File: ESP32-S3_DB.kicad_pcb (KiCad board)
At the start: 4 copper layers, 123.5 x 56.5 mm, 157 parts, among them CN1 JST_Battery, J1 TYPE-C-31-M12_13, J10 U2RS485_TX, J11 CAN_TX, J12 CAN_RX, J14 Conn_01x06, J15 Conn_01x10, J16 Conn_01x08, J17 U2RS485_RX, J18 U2RS485_DE_~{RE}, J19 U2RS485_TX, J2 A - B, J20 U2RS485_RX, J21 U2U, J22 PROG_Default, J3 H - L, J4 TYPE-C-31-M12_13, J5 EXT_LOAD, J6 R4_TX, J7 R4_RX, J8 Micro_SD_Card_Det1, J9 Conn_01x06, SW1 RESET, SW2 BOOT, SW3 ON/OFF, U1 ESP32-S3FH4R2, U2 UMH3N, U3 IP5306, U4 CH340X, U5 LD1117DT33CTR, U6 SP3071EEN-L/TR, U7 ATA6561-GAQW-N, X1 32.768KHz, Y1 40MHz

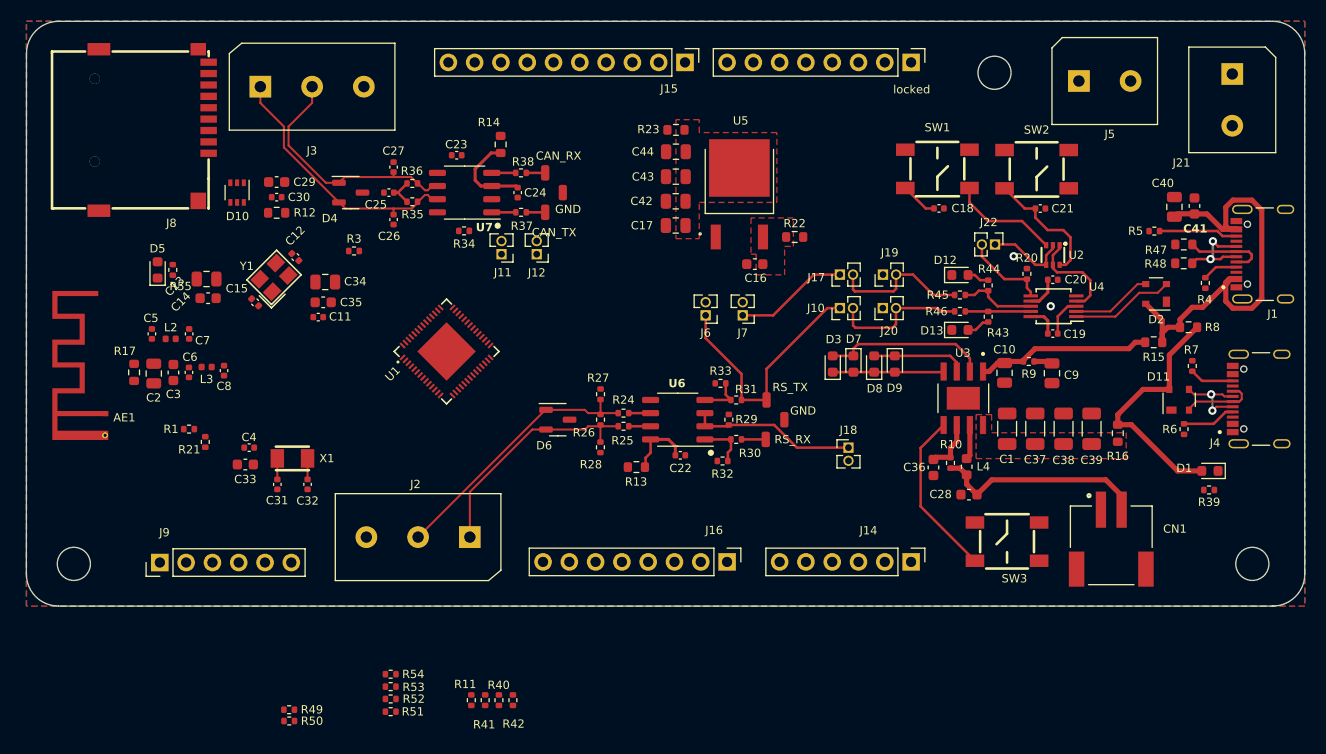
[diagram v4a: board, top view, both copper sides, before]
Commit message: Completed routing for all GPIO pins
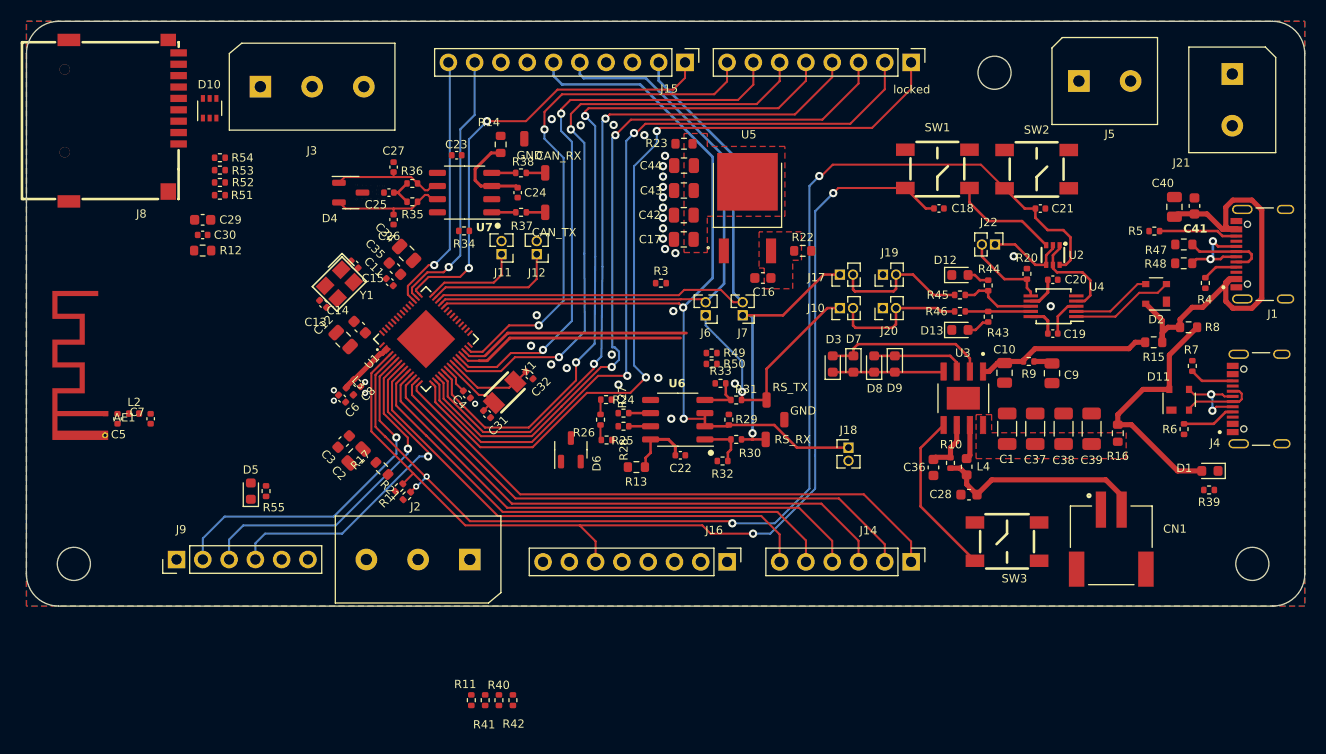
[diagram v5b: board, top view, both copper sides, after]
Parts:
- removed C33: 1uF, ESP32-S3_Dev_Board:C_0603_1608Metric
- moved R50 53.4 mm to (158.7, 119.1)
- moved R49 53.4 mm to (158.7, 118.0)
- moved R52 52.6 mm to (111.2, 101.6)
- moved R53 52.6 mm to (111.2, 100.4)
- moved R54 52.6 mm to (111.2, 99.2)
- moved R51 52.6 mm to (111.2, 102.8)
- moved R3 29.8 mm to (153.8, 111.3)
- moved R17 25.7 mm to (126.8, 129.2), turned to 135 degrees
- moved C32 23.9 mm to (141.1, 120.2), turned to -45 degrees
- moved D5 23.2 mm to (114.2, 131.4)
- moved R55 23.2 mm to (115.7, 131.4)
- moved C4 21.6 mm to (135.1, 122.0), turned to -45 degrees
- moved X1 21.5 mm to (138.7, 121.8), turned to 45 degrees
- moved C31 21.4 mm to (137.0, 124.0), turned to -45 degrees
- moved C2 21.1 mm to (124.3, 128.0), turned to -135 degrees
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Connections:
- J10 pad 2: /U2U_RXD -> /U2U_TXD
- J14 pad 1: /GPIO11 -> /GPIO9
- J14 pad 2: /GPIO10 -> /GPIO8
- J14 pad 3: /GPIO9 -> /GPIO7
- J14 pad 4: /GPIO8 -> /GPIO6
- J14 pad 5: /GPIO7 -> /GPIO5
- J14 pad 6: /GPIO6 -> /GPIO4
- J15 pad 1: /GPIO9 -> /GPIO38
- J15 pad 10: /GPIO39 -> /GPIO40
- J15 pad 2: /EXTERNAL CONNECTORS/GPIO14 -> /RS485_RX/GPIO34
- J15 pad 5: /EXTERNAL CONNECTORS/GPIO17 -> /RS485_TX/GPIO33
- J15 pad 6: /GPIO18 -> /RS485_~{RE}_DE/GPIO35
- J15 pad 9: /GPIO38 -> /GPIO39
- J17 pad 2: /U2U_TXD -> /U2U_RXD
- J6 pad 2: /RS-485_RX/GPIO46 -> /RS485_TX/GPIO33
- J7 pad 2: /RS-485_TX/GPIO45 -> /RS485_RX/GPIO34
- J9 pad 5: /GPIO4 -> unconnected-(J9-Pin_5-Pad5)
- J9 pad 6: /GPIO5 -> unconnected-(J9-Pin_6-Pad6)
- R51 pad 1: /~{MCU_SL_CS} -> /MCU_SL_CLK
- R51 pad 2: unconnected-(R51-Pad2) -> Net-(U1-MTDI)
- R52 pad 1: /MCU_SL_MISO -> /MCU_SL_MOSI
- R52 pad 2: unconnected-(R52-Pad2) -> Net-(U1-MTMS)
- R53 pad 1: /MCU_SL_CLK -> /MCU_SL_MISO
- R53 pad 2: unconnected-(R53-Pad2) -> Net-(U1-GPIO45)
- R54 pad 1: /MCU_SL_MOSI -> /~{MCU_SL_CS}
- R54 pad 2: unconnected-(R54-Pad2) -> Net-(U1-GPIO46)
- U1 pad 19: /ESP32-S3/GPIO 14 -> /GPIO14
- U1 pad 23: /ESP32-S3/GPIO 17 -> /GPIO17
- U1 pad 27: /ESP32-S3/GPIO 21 -> /GPIO21
- U1 pad 38: /ESP32-S3/RS-485_TX/GPIO33 -> /RS485_~{RE}_DE/GPIO35
- U1 pad 39: /ESP32-S3/RS-485_RX/GPIO34 -> /RS485_TX/GPIO33
- U1 pad 40: /CAN_RXD/GPIO35 -> /RS485_RX/GPIO34
- U1 pad 41: /RS485_~{RE}_DE/GPIO35 -> /CAN_RXD/GPIO35
- U1 pad 47: /GPIO41 -> Net-(U1-MTDI)
- U1 pad 48: unconnected-(U1-MTMS-Pad48) -> Net-(U1-MTMS)
- U1 pad 51: unconnected-(U1-GPIO45-Pad51) -> Net-(U1-GPIO45)
- U1 pad 52: unconnected-(U1-GPIO46-Pad52) -> Net-(U1-GPIO46)
- locked pad 1: /GPIO21 -> /GPIO10
- locked pad 2: /GPIO33 -> /GPIO11
- locked pad 3: /GPIO34 -> /GPIO12
- locked pad 4: /GPIO35 -> /GPIO13
- locked pad 5: /GPIO36 -> /GPIO14
- locked pad 6: /GPIO37 -> /GPIO17
- locked pad 7: /EXTERNAL CONNECTORS/CAN_RX/GPIO8 -> /GPIO18
- locked pad 8: /EXTERNAL CONNECTORS/CAN_TX/GPIO7 -> /GPIO21
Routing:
- net /BOOT: track 12.3 -> 119.1 mm, vias 0 -> 4
- net /RESET: track 14.1 -> 113.2 mm, vias 0 -> 2
- net /GPIO10: track 0.00 -> 80.9 mm, vias 0 -> 2
- net /GPIO11: track 0.00 -> 77.0 mm, vias 0 -> 2
- net /GPIO12: track 0.00 -> 73.7 mm, vias 0 -> 2
- net /RS485_~{RE}_DE/GPIO35: track 16.1 -> 88.0 mm, vias 0 -> 2
- net /GPIO13: track 0.00 -> 70.1 mm, vias 0 -> 2
- net /GPIO14: track 0.00 -> 69.2 mm, vias 0 -> 2
- net /GPIO17: track 0.00 -> 59.4 mm, vias 0 -> 2
- net /RS485_TX/GPIO33: track 0.00 -> 59.1 mm
- net /RS485_RX/GPIO34: track 0.00 -> 56.9 mm
- net /GPIO9: track 0.00 -> 56.7 mm
- net /GPIO18: track 0.00 -> 55.8 mm, vias 0 -> 2
- net /GPIO8: track 0.00 -> 55.0 mm
- net /GPIO7: track 0.00 -> 53.8 mm
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
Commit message: Completed RS485 and CAN routing
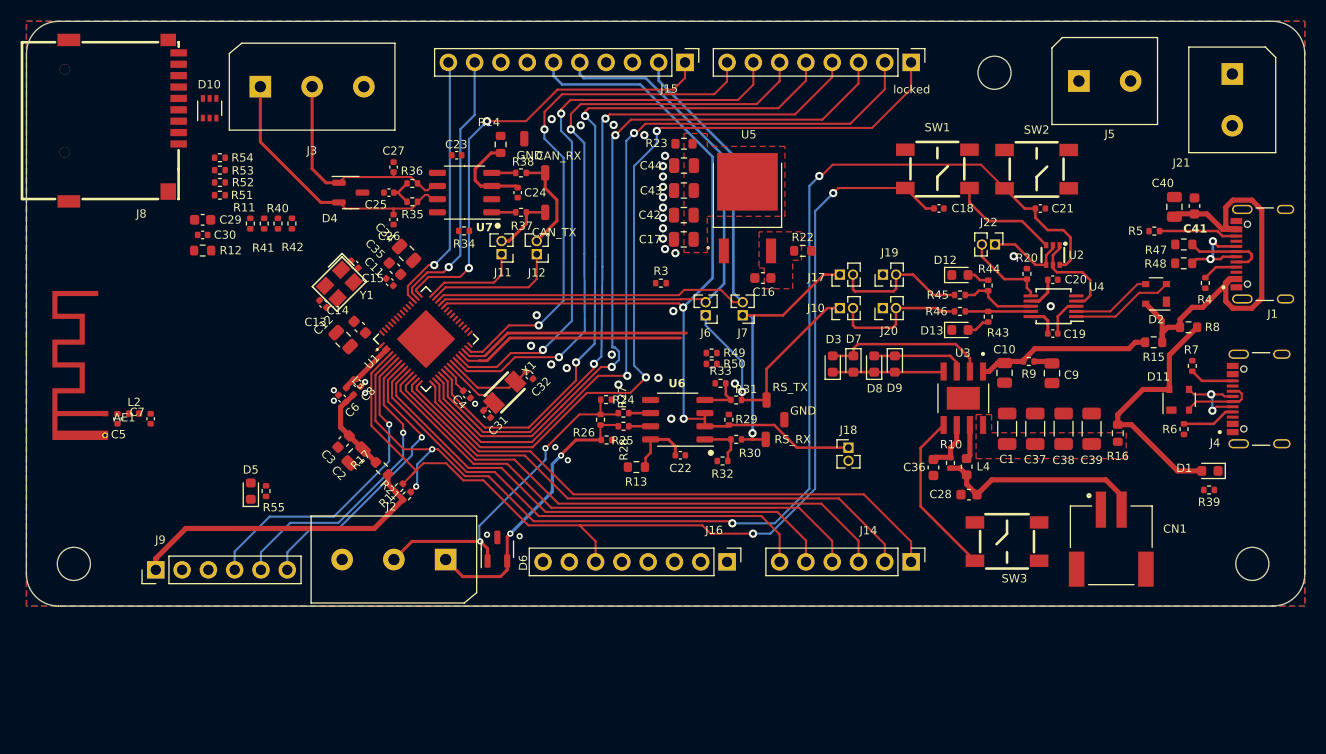
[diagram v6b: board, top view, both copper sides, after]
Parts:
- moved R40 50.8 mm to (116.8, 105.5)
- moved R11 50.8 mm to (114.1, 105.5)
- moved R41 50.8 mm to (115.5, 105.5)
- moved R42 50.8 mm to (118.2, 105.5)
- moved D6 11.9 mm to (138.0, 137.0)
- moved J2 2.34 mm to (128.0, 138.0)
- moved J9 2.24 mm to (105.0, 139.0)
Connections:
- D6 pad 2: /RS_485/COMM_RS485_B -> /CONN_RS485_B
- J9 pad 2: /GPIO1 -> GND
- J9 pad 3: /GPIO2 -> unconnected-(J9-Pin_3-Pad3)
- J9 pad 4: /GPIO3 -> /GPIO1
- J9 pad 5: unconnected-(J9-Pin_5-Pad5) -> /GPIO2
- J9 pad 6: unconnected-(J9-Pin_6-Pad6) -> /GPIO3
- R25 pad 2: /RS_485/COMM_RS485_B -> /CONN_RS485_B
- R26 pad 1: /RS_485/COMM_RS485_B -> /CONN_RS485_B
- R28 pad 2: /RS_485/COMM_RS485_B -> /CONN_RS485_B
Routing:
- net /CONN_RS485_A: track 1.44 -> 32.8 mm, vias 0 -> 2
- net /3V3: track 2.85 -> 33.2 mm
- net /CONN_RS485_B: track 0.00 -> 28.1 mm, vias 0 -> 2
- net /CONN_CANH: track 11.0 -> 26.4 mm
- net /CONN_CANL: track 10.9 -> 22.0 mm
- net Net-(C2-Pad1): track 0.00 -> 8.49 mm
- net /CAN_TRANS_RXD: track 1.83 -> 9.69 mm
- net /CAN_TRANS_TXD: track 1.82 -> 6.01 mm
- net /GPIO3: track 32.7 -> 28.6 mm
- net /GPIO1: track 34.6 -> 31.2 mm
- net /GPIO2: track 33.0 -> 29.9 mm
- net /BOOT: track 119.1 -> 121.5 mm
- net /RS_485/COMM_RS485_B: track 1.65 -> 0.00 mm
- net /RESET: track 113.2 -> 114.2 mm
- net Net-(U1-LNA_IN): track 0.03 -> 0.87 mm
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
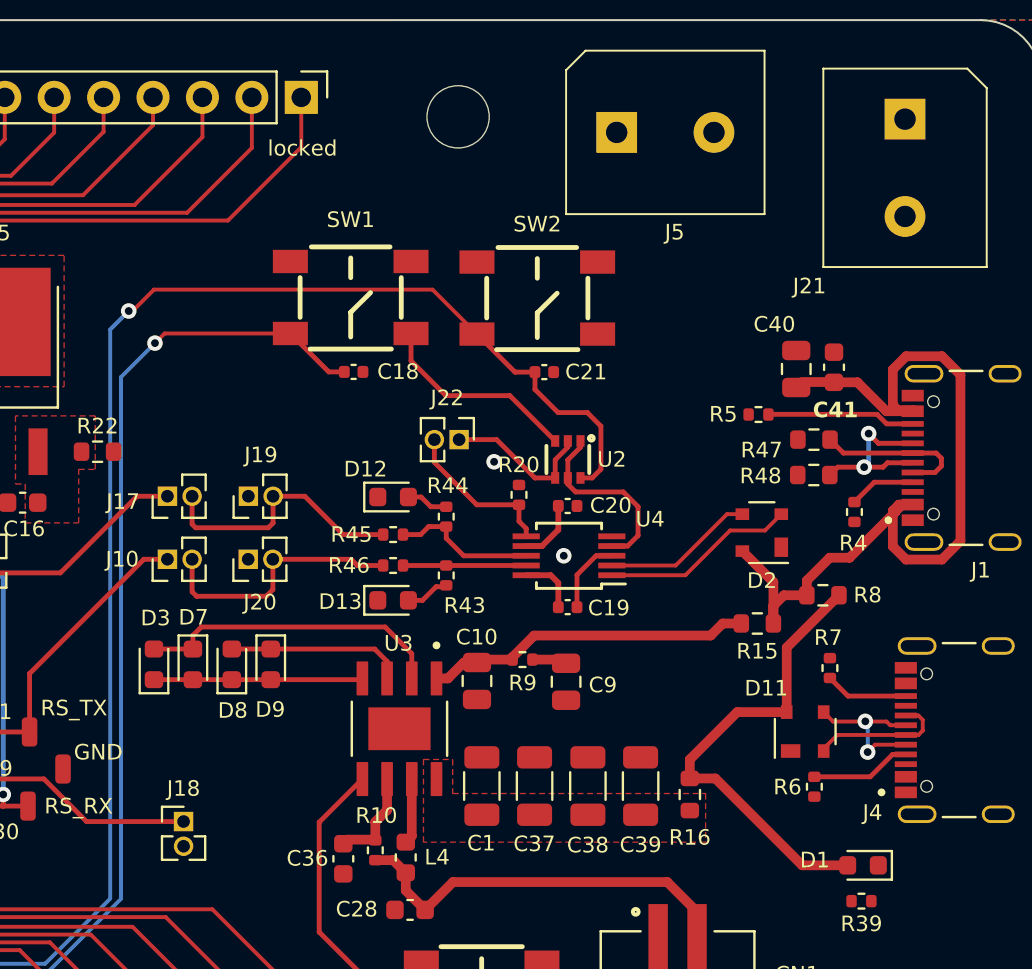
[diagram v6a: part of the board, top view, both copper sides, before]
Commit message: Completed routing for USB peripheral for CH340
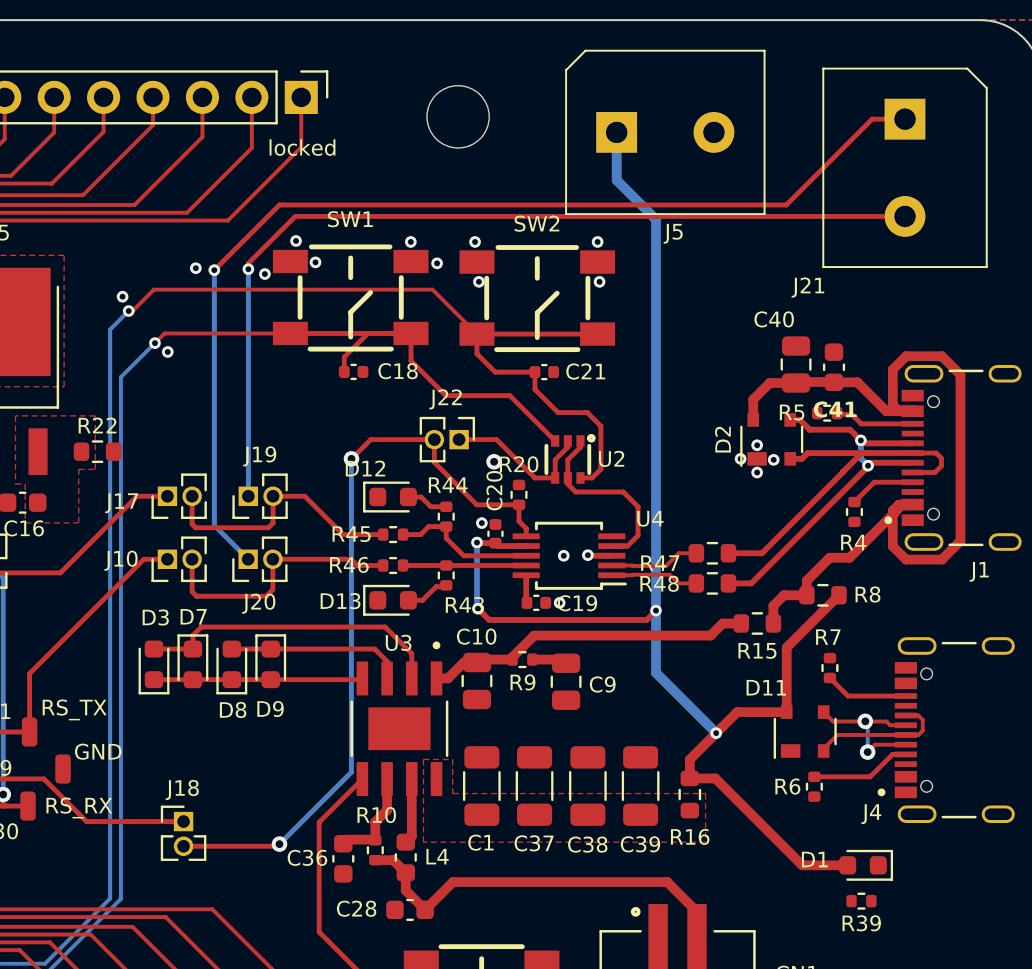
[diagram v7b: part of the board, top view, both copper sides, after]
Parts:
- moved R47 7.83 mm to (199.1, 113.4)
- moved R48 7.63 mm to (199.1, 115.0)
- moved D2 4.82 mm to (202.2, 107.5), turned to 90 degrees
- moved C20 3.98 mm to (187.9, 112.4), turned to -90 degrees
- moved R5 3.53 mm to (205.0, 106.2)
- moved C19 1.62 mm to (190.1, 116.0)
- moved C40 0.23 mm to (203.4, 103.7)
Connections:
- D2 pad 2: /D+ -> /INPUT POWER/DN
- D2 pad 3: /D- -> /INPUT POWER/DP
- J1 pad A6: Net-(J1-D+-PadA6) -> /INPUT POWER/DP
- J1 pad A7: Net-(J1-D--PadA7) -> /INPUT POWER/DN
- J1 pad B6: Net-(J1-D+-PadA6) -> /INPUT POWER/DP
- J1 pad B7: Net-(J1-D--PadA7) -> /INPUT POWER/DN
- J21 pad 1: /U2U_CONN_TX -> /U2U_CONN_RX
- J21 pad 2: /U2U_CONN_RX -> /U2U_CONN_TX
- R47 pad 1: Net-(J1-D--PadA7) -> /INPUT POWER/DN
- R48 pad 1: Net-(J1-D+-PadA6) -> /INPUT POWER/DP
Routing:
- net /U2U_CONN_RX: track 0.00 -> 54.3 mm, vias 0 -> 1
- net /U2U_CONN_TX: track 0.00 -> 46.7 mm, vias 0 -> 1
- net /5V: track 27.3 -> 72.7 mm, vias 0 -> 4
- net /TNOW: track 8.20 -> 39.2 mm, vias 0 -> 2
- net /INPUT POWER/DP: track 0.00 -> 20.3 mm, vias 0 -> 2
- net /INPUT POWER/DN: track 0.00 -> 19.3 mm
- net Net-(J1-D+-PadA6): track 8.81 -> 0.00 mm, vias 2 -> 0
- net Net-(J1-D--PadA7): track 8.13 -> 0.00 mm
- net /RESET: track 114.2 -> 121.6 mm
- net /BOOT: track 121.5 -> 128.3 mm
- net /D+: track 10.0 -> 4.54 mm
- net /INPUT POWER/CC2: track 7.62 -> 4.11 mm
- net /D-: track 7.80 -> 4.63 mm
- net GND: track 3.86 -> 1.41 mm, vias 51 -> 70
- net /USB-TO-UART/V3: track 3.06 -> 1.44 mm
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
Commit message: Merge changes upstream
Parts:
- removed C34: 10uF, ESP32-S3_Dev_Board:C_0805_2012Metric
- removed C35: 1uF, ESP32-S3_Dev_Board:C_0603_1608Metric
- removed R3: 500, ESP32-S3_Dev_Board:R_0402_1005Metric
- added R2: 270, ESP32-S3_Dev_Board:R_0402_1005Metric, F.Cu at (137.7, 113.8)
- moved J9 63.1 mm to (162.9, 113.9), turned to 0 degrees
- moved R52 47.6 mm to (151.3, 127.1), turned to 135 degrees
- moved R51 46.1 mm to (150.1, 127.6), turned to 135 degrees
- moved R54 44.7 mm to (148.3, 124.1), turned to 135 degrees
- moved R53 43.9 mm to (147.5, 125.0), turned to 135 degrees
- moved R28 40.8 mm to (107.7, 126.9), turned to 90 degrees
- moved R27 40.8 mm to (107.7, 121.8), turned to 90 degrees
- moved R50 40.3 mm to (199.0, 119.5), turned to 90 degrees
- moved C22 40.2 mm to (115.5, 127.7)
- moved R13 40.2 mm to (111.2, 128.9)
- moved R24 40.2 mm to (110.0, 123.6)
- moved R25 40.2 mm to (110.0, 124.9)
- moved R26 40.2 mm to (107.7, 124.3)
- moved R29 40.2 mm to (120.1, 124.3)
- moved R33 40.2 mm to (119.3, 120.8)
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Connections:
- net /CONN_CANH renamed /CAN_P
- net /CONN_CANL renamed /CAN_N
- net /CONN_RS485_A renamed /RS485_P
- net /CONN_RS485_B renamed /RS485_N
- net /RS_485/RS485_A renamed /RS_485/RS_485_P
- net /RS_485/RS485_B renamed /RS_485/RS_485_N
- net Net-(U1-XTAL_32K_N) renamed /ESP32-S3/XTALN
- net Net-(U1-XTAL_32K_P) renamed /ESP32-S3/XTALP
- D2 pad 2: /INPUT POWER/DN -> /D+
- D2 pad 3: /INPUT POWER/DP -> /D-
- J1 pad A6: /INPUT POWER/DP -> Net-(J1-D+-PadA6)
- J1 pad A7: /INPUT POWER/DN -> Net-(J1-D--PadA7)
- J1 pad B6: /INPUT POWER/DP -> Net-(J1-D+-PadA6)
- J1 pad B7: /INPUT POWER/DN -> Net-(J1-D--PadA7)
- J10 pad 2: /U2U_TXD -> /U2U_RXD
- J11 pad 1: /CAN_TXD/GPIO36 -> /CAN_TXD/GPIO7
- J12 pad 1: /CAN_RXD/GPIO35 -> /CAN_RXD/GPIO8
- J14 pad 1: /GPIO9 -> /GPIO6
- J14 pad 2: /GPIO8 -> /GPIO5
- J14 pad 3: /GPIO7 -> /GPIO4
- J14 pad 4: /GPIO6 -> /GPIO3
- J14 pad 5: /GPIO5 -> /GPIO2
- J14 pad 6: /GPIO4 -> /GPIO1
- J15 pad 1: /GPIO38 -> /GPIO9
- J15 pad 10: /GPIO40 -> /GPIO39
- J15 pad 2: /RS485_RX/GPIO34 -> /GPIO14
- J15 pad 4: unconnected-(J15-Pin_4-Pad4) -> /GPIO41
- J15 pad 5: /RS485_TX/GPIO33 -> /GPIO17
- J15 pad 6: /RS485_~{RE}_DE/GPIO35 -> /GPIO18
- J15 pad 8: unconnected-(J15-Pin_8-Pad8) -> /GPIO40
- J15 pad 9: /GPIO39 -> /GPIO38
- J16 pad 8: unconnected-(J16-Pin_8-Pad8) -> /R4_~{RE}_DE
- J17 pad 2: /U2U_RXD -> /U2U_TXD
- J18 pad 1: /RS485_~{RE}_DE/GPIO35 -> /R4_~{RE}_DE
- J21 pad 1: /U2U_CONN_RX -> /U2U_CONN_TX
- J21 pad 2: /U2U_CONN_TX -> /U2U_CONN_RX
- J6 pad 2: /RS485_TX/GPIO33 -> /RS-485_RX/GPIO46
- J7 pad 2: /RS485_RX/GPIO34 -> /RS-485_TX/GPIO45
- J9 pad 1: /3V3 -> /RS-485_TX/GPIO45
- J9 pad 2: GND -> /RS-485_RX/GPIO46
- J9 pad 4: /GPIO1 -> /3V3
- J9 pad 5: /GPIO2 -> unconnected-(J9-Pin_5-Pad5)
- J9 pad 6: /GPIO3 -> unconnected-(J9-Pin_6-Pad6)
- R29 pad 2: /RS485_~{RE}_DE/GPIO35 -> /R4_~{RE}_DE
- R47 pad 1: /INPUT POWER/DN -> Net-(J1-D--PadA7)
- R48 pad 1: /INPUT POWER/DP -> Net-(J1-D+-PadA6)
- R51 pad 1: /MCU_SL_CLK -> /~{MCU_SL_CS}
- R51 pad 2: Net-(U1-MTDI) -> Net-(U1-GPIO10)
- R52 pad 1: /MCU_SL_MOSI -> /MCU_SL_MISO
- R52 pad 2: Net-(U1-MTMS) -> Net-(U1-GPIO11)
- R53 pad 1: /MCU_SL_MISO -> /MCU_SL_CLK
- R53 pad 2: Net-(U1-GPIO45) -> Net-(U1-GPIO12)
- R54 pad 1: /~{MCU_SL_CS} -> /MCU_SL_MOSI
- R54 pad 2: Net-(U1-GPIO46) -> Net-(U1-GPIO13)
- U1 pad 12: /GPIO7 -> /U2U_RXD
- U1 pad 13: /GPIO8 -> /U2U_TXD
- U1 pad 14: /GPIO9 -> /R4_~{RE}_DE
- U1 pad 15: /GPIO10 -> Net-(U1-GPIO10)
- U1 pad 16: /GPIO11 -> Net-(U1-GPIO11)
- U1 pad 17: /GPIO12 -> Net-(U1-GPIO12)
- U1 pad 18: /GPIO13 -> Net-(U1-GPIO13)
- U1 pad 38: /RS485_~{RE}_DE/GPIO35 -> /GPIO33
- U1 pad 39: /RS485_TX/GPIO33 -> /GPIO34
- U1 pad 40: /RS485_RX/GPIO34 -> /GPIO35
- U1 pad 41: /CAN_RXD/GPIO35 -> /GPIO36
- U1 pad 42: /CAN_TXD/GPIO36 -> /GPIO37
- U1 pad 47: Net-(U1-MTDI) -> /GPIO41
- U1 pad 48: Net-(U1-MTMS) -> /GPIO9
- U1 pad 49: Net-(U1-U0TXD) -> /CAN_TXD/GPIO7
- U1 pad 50: /U2U_TXD -> /CAN_RXD/GPIO8
- U1 pad 51: Net-(U1-GPIO45) -> /RS-485_TX/GPIO45
- U1 pad 52: Net-(U1-GPIO46) -> /RS-485_RX/GPIO46
- U6 pad 2: /RS485_~{RE}_DE/GPIO35 -> /R4_~{RE}_DE
- U6 pad 3: /RS485_~{RE}_DE/GPIO35 -> /R4_~{RE}_DE
- locked pad 1: /GPIO10 -> /GPIO21
- locked pad 2: /GPIO11 -> /GPIO33
- locked pad 3: /GPIO12 -> /GPIO34
- locked pad 4: /GPIO13 -> /GPIO35
- locked pad 5: /GPIO14 -> /GPIO36
- locked pad 6: /GPIO17 -> /GPIO37
- locked pad 7: /GPIO18 -> /CAN_RXD/GPIO8
- locked pad 8: /GPIO21 -> /CAN_TXD/GPIO7
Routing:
- net /BOOT: track 128.3 -> 15.6 mm, vias 4 -> 0
- net /RESET: track 121.6 -> 17.7 mm, vias 2 -> 0
- net /RS485_~{RE}_DE/GPIO35: track 88.0 -> 0.00 mm, vias 2 -> 0
- net /GPIO10: track 80.9 -> 0.00 mm, vias 2 -> 0
- net /GPIO11: track 77.0 -> 0.00 mm, vias 2 -> 0
- net /GPIO12: track 73.7 -> 0.00 mm, vias 2 -> 0
- net /GPIO13: track 70.1 -> 0.00 mm, vias 2 -> 0
- net /RS485_TX/GPIO33: track 59.1 -> 0.00 mm
- net /RS485_RX/GPIO34: track 56.9 -> 0.00 mm
- net /GPIO8: track 54.7 -> 0.00 mm
- net /U2U_CONN_RX: track 54.3 -> 0.00 mm, vias 1 -> 0
- net /CAN_RXD/GPIO8: track 0.00 -> 53.7 mm, vias 0 -> 1
- net /GPIO7: track 53.4 -> 0.00 mm
- net /U2U_CONN_TX: track 46.7 -> 0.00 mm, vias 1 -> 0
- net /CAN_TXD/GPIO7: track 0.00 -> 45.6 mm
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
